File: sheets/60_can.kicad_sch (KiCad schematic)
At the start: 1 part, among them U1 ADM3055E

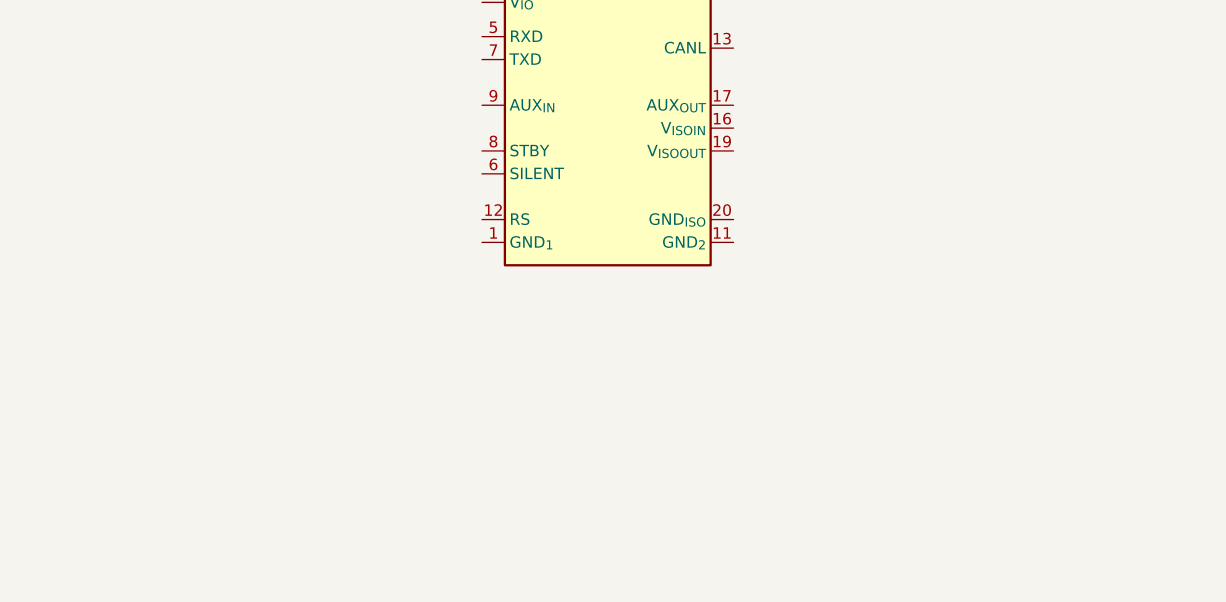
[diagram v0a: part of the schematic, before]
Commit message: Corrige la base del esquemático y añade reglas de proyecto
- Extrae el símbolo ADM3055E a lib/antmicro_adm3055ebriz.kicad_sym y lo
  registra en sym-lib-table con ${KIPRJMOD}.
- U1: huella Package_SO:SOIC-20W_7.5x12.8mm_P1.27mm (nota: verificar
  land pattern contra el datasheet).
- 10_power_input: power:GND -> GND_VEH; huellas y MPN de C1, C2 (0805
  X7R 100 V automotriz), C3 (EEE-HA2A470UP, 10x10) y F1 (1812, MPN
  pendiente).
- Nuevos pines jerárquicos CAN_SILENT (40_mcu -> 60_can, pull-down R1
  10k a GND_ISO) e IMU_INT2 (50_sensors -> 40_mcu).
- CLAUDE.md con reglas de librerías, campos, conexiones entre hojas,
  verificación por hoja y versión prototipo.
- Ignora output/ (reportes generados por kicad-mcp).

Co-Authored-By: Claude Opus 5.5 <noreply@anthropic.com>
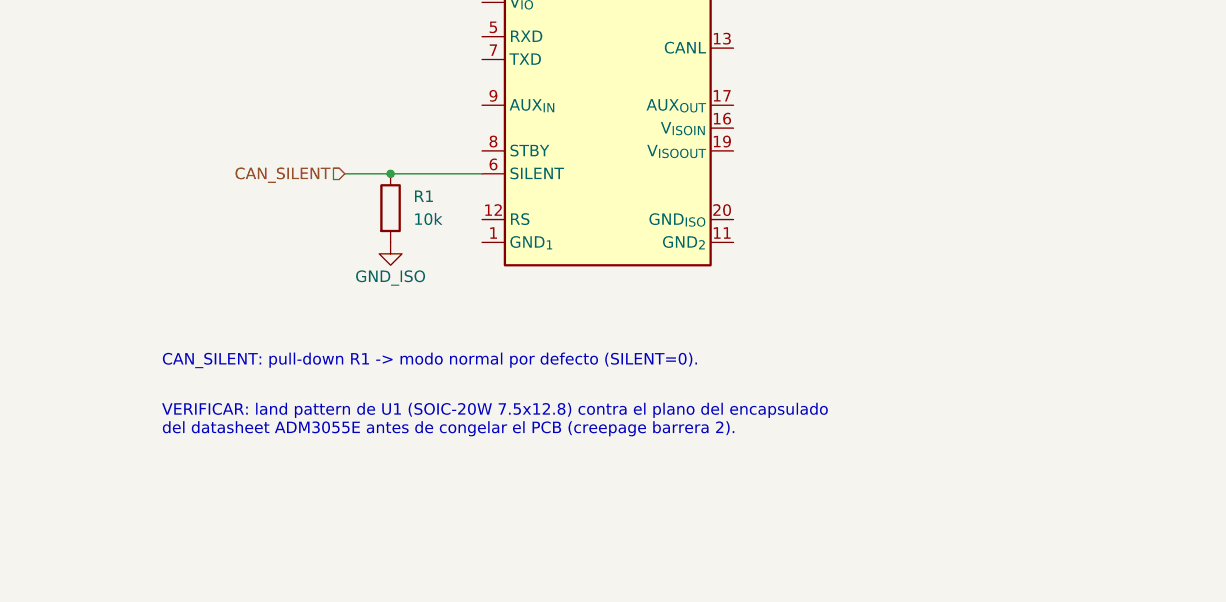
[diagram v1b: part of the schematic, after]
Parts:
- added R1: 10k, Resistor_SMD:R_0603_1608Metric, symbol Device:R
- U1: footprint ADM3055E -> Package_SO:SOIC-20W_7.5x12.8mm_P1.27mm
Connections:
- net GND_ISO: now also R1.2
- net CAN_SILENT: now reaches U1.6 (SILENT)
- net CAN_SILENT: now also R1.1
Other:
- note added: "CAN_SILENT: pull-down R1 -> modo normal por defecto (SILENT=0)."
- note added: "VERIFICAR: land pattern de U1 (SOIC-20W 7.5x12.8) contra el plano del encapsulado del datasheet ADM3055E antes de congelar el PCB (creepage barrera 2)."
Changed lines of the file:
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@@
 			)
 		)
-		(property "Footprint" "ADM3055E"
+		(property "Footprint" "Package_SO:SOIC-20W_7.5x12.8mm_P1.27mm"
 			(at 196.85 130.81 0)
 			(hide yes)
@@
 					(unit 1)
 				)
+			)
+		)
+	)
+	(wire
+		(pts
+			(xy 156.21 146.05) (xy 140.97 146.05)
+		)
+		(stroke
+			(width 0)
+			(type default)
+		)
+	)
+	(junction
+		(at 146.05 146.05)
+		(diameter 0)
+		(color 0 0 0 0)
+	)
+	(hierarchical_label "CAN_SILENT"
+		(shape input)
+		(at 140.97 146.05 180)
+		(effects
+			(font
+				(size 1.27 1.27)
+			)
+			(justify right)
+		)
+	)
+	(text "CAN_SILENT: pull-down R1 -> modo normal por defecto (SILENT=0)."
+		(exclude_from_sim no)
+		(at 120.65 167.64 0)
+		(effects
+			(font
+				(size 1.27 1.27)
+			)
+			(justify left bottom)
+		)
+	)
+	(text "VERIFICAR: land pattern de U1 (SOIC-20W 7.5x12.8) contra el plano del encapsulado\ndel datasheet ADM3055E antes de congelar el PCB (creepage barrera 2)."
+		(exclude_from_sim no)
+		(at 120.65 175.26 0)
+		(effects
+			(font
+				(size 1.27 1.27)
+			)
+			(justify left bottom)
+		)
+	)
+	(symbol
+		(lib_id "Device:R")
+		(at 146.05 149.86 0)
+		(unit 1)
+		(body_style 1)
+		(exclude_from_sim no)
+		(in_bom yes)
+		(on_board yes)
+		(in_pos_files yes)
+		(dnp no)
+		(property "Reference" "R1"
+			(at 148.59 148.59 0)
+			(show_name no)
+			(do_not_autoplace no)
+			(effects
+				(font
+					(size 1.27 1.27)
+				)
+				(justify left)
+			)
+		)
+		(property "Value" "10k"
+			(at 148.59 151.13 0)
+			(show_name no)
+			(do_not_autoplace no)
+			(effects
+				(font
+					(size 1.27 1.27)
+				)
+				(justify left)
+			)
+		)
+		(property "Footprint" "Resistor_SMD:R_0603_1608Metric"
+			(at 146.05 149.86 0)
+			(hide yes)
+			(show_name no)
+			(do_not_autoplace no)
+			(effects
+				(font
+					(size 1.27 1.27)
+				)
+			)
+		)
+		(property "Datasheet" "https://www.yageo.com/upload/media/product/productsearch/datasheet/rchip/PYu-AC_51_RoHS_L_12.pdf"
+			(at 146.05 149.86 0)
+			(hide yes)
+			(show_name no)
+			(do_not_autoplace no)
+			(effects
+				(font
+					(size 1.27 1.27)
+				)
+			)
+		)
+		(property "Description" "Pull-down SILENT del ADM3055E (modo normal por defecto)"
+			(at 146.05 149.86 0)
+			(hide yes)
+			(show_name no)
+			(do_not_autoplace no)
+			(effects
+				(font
+					(size 1.27 1.27)
+				)
+			)
+		)
+		(property "MPN" "AC0603FR-0710KL"
+			(at 146.05 149.86 0)
+			(hide yes)
+			(show_name no)
+			(do_not_autoplace no)
+			(effects
+				(font
+					(size 1.27 1.27)
+				)
+			)
+		)
+		(property "Manufacturer" "Yageo"
+			(at 146.05 149.86 0)
+			(hide yes)
+			(show_name no)
+			(do_not_autoplace no)
+			(effects
+				(font
+					(size 1.27 1.27)
+				)
+			)
+		)
+		(pin "1"
+		)
+		(pin "2"
+		)
+		(instances
+			(project "INCLI-VA"
+				(path "/7fd92c2b-4254-4d73-93ba-bfde861bede3/3036af0c-b072-4a36-8ec1-d374aba21569"
+					(reference "R1")
+					(unit 1)
+				)
+			)
+		)
+	)
+	(symbol
+		(lib_id "INCLI-VA:GND_ISO")
+		(at 146.05 153.67 0)
+		(unit 1)
+		(body_style 1)
+		(exclude_from_sim no)
+		(in_bom no)
+		(on_board yes)
+		(in_pos_files yes)
+		(dnp no)
+		(property "Reference" "#PWR032"
+			(at 146.05 160.02 0)
+			(hide yes)
+			(show_name no)
+			(do_not_autoplace no)
+			(effects
+				(font
+					(size 1.27 1.27)
+				)
+			)
+		)
+		(property "Value" "GND_ISO"
+			(at 146.05 157.48 0)
+			(show_name no)
+			(do_not_autoplace no)
+			(effects
+				(font
+					(size 1.27 1.27)
+				)
+			)
+		)
+		(property "Footprint" ""
+			(at 146.05 153.67 0)
+			(hide yes)
+			(show_name no)
+			(do_not_autoplace no)
+			(effects
+				(font
+					(size 1.27 1.27)
+				)
+			)
+		)
+		(property "Datasheet" ""
+			(at 146.05 153.67 0)
+			(hide yes)
+			(show_name no)
+			(do_not_autoplace no)
+			(effects
+				(font
+					(size 1.27 1.27)
+				)
+			)
+		)
+		(pin "1"
+		)
+		(instances
+			(project "INCLI-VA"
+				(path "/7fd92c2b-4254-4d73-93ba-bfde861bede3/3036af0c-b072-4a36-8ec1-d374aba21569"
+					(reference "#PWR032")
+					(unit 1)
+				)
